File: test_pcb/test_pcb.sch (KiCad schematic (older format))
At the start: 69 parts, among them K0 KEYSW, K1 KEYSW, K10 KEYSW, K12 KEYSW, K13 KEYSW, K14 KEYSW, K15 KEYSW, K16 KEYSW, K17 KEYSW, K18 KEYSW, K2 KEYSW, K20 KEYSW, K21 KEYSW, K22 KEYSW, K3 KEYSW, K4 KEYSW, K5 KEYSW, K6 KEYSW, K7 KEYSW, K8 KEYSW, K9 KEYSW, P0 CONN_01X08, U0 Teensy3.2, U1 STP16CP05

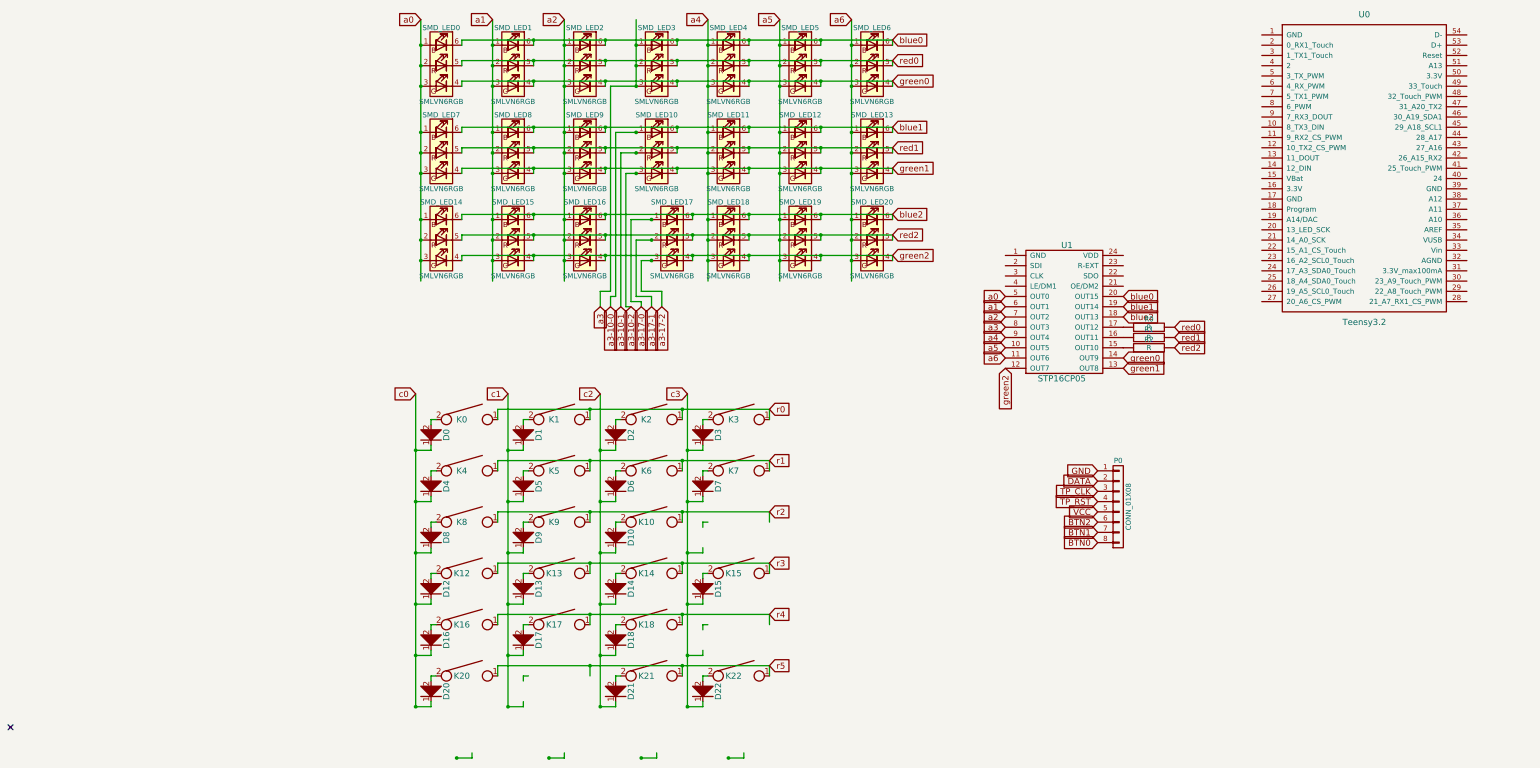
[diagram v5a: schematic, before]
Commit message: ground planes added
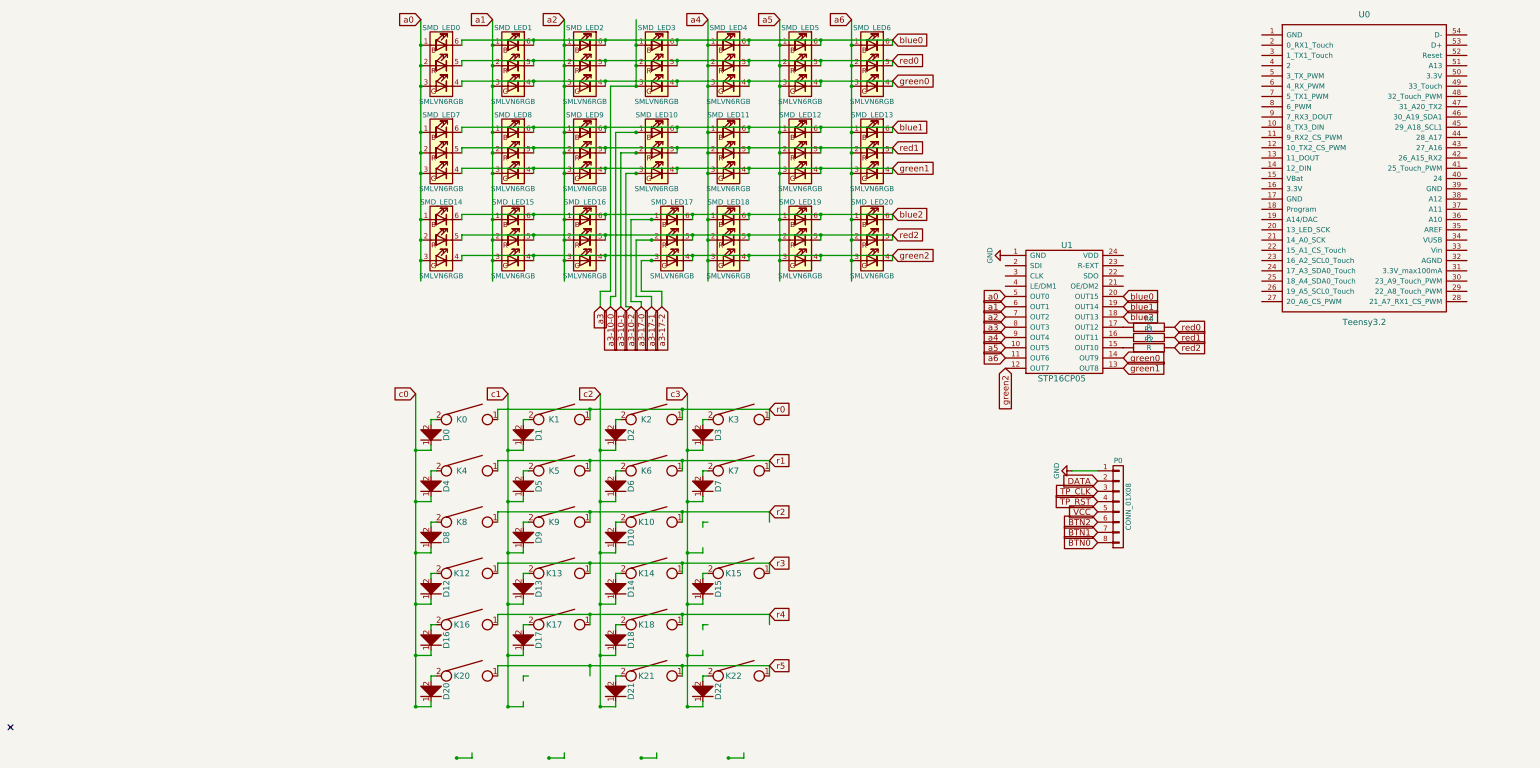
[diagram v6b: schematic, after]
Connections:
- wire segments 375 -> 243

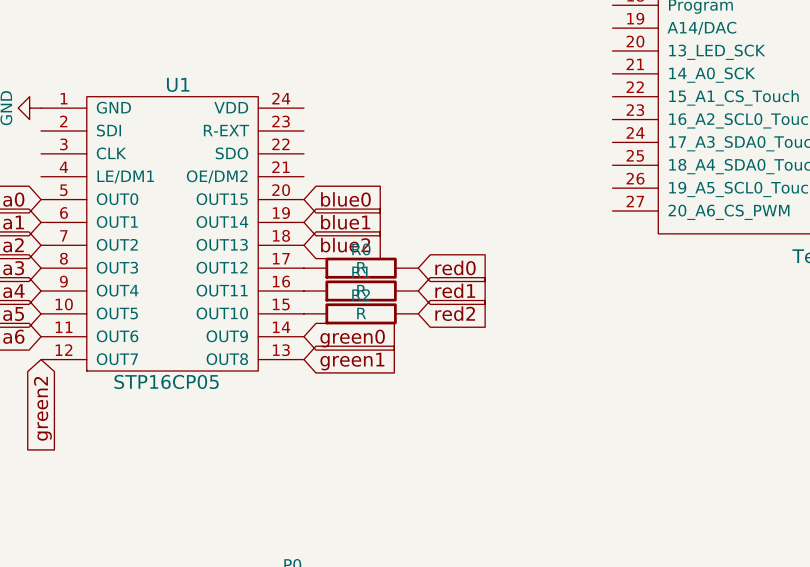
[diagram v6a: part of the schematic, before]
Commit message: when you use a contant current LED driver you don't actually need resistors!
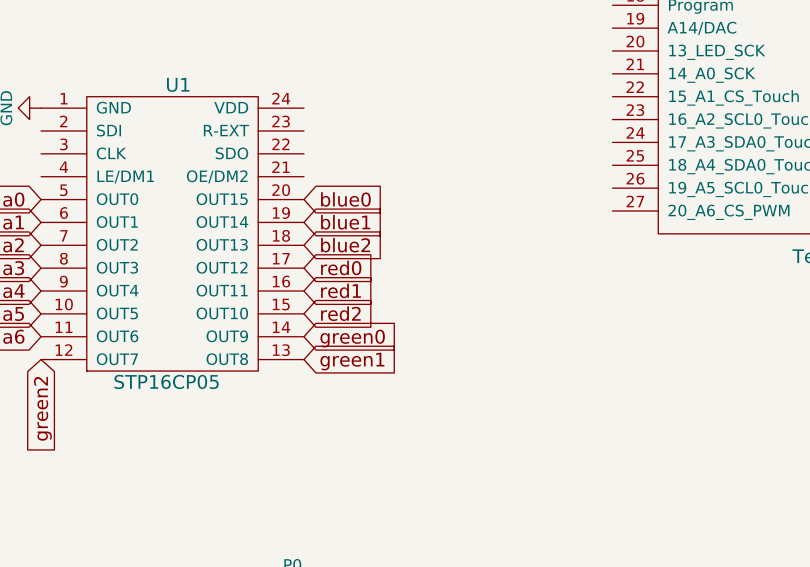
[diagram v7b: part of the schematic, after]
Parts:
- removed R0, R1, R2: R, Resistors_SMD:R_0603_HandSoldering, symbol R
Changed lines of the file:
@@
 Text GLabel 7650 3250 2    60   Input ~ 0
 blue0
-Text GLabel 8150 3550 2    60   Input ~ 0
+Text GLabel 7650 3550 2    60   Input ~ 0
 red0
 Text GLabel 7650 3850 2    60   Input ~ 0
@@
 Text GLabel 7650 3350 2    60   Input ~ 0
 blue1
-Text GLabel 8150 3650 2    60   Input ~ 0
+Text GLabel 7650 3650 2    60   Input ~ 0
 red1
 Text GLabel 7650 3950 2    60   Input ~ 0
@@
 Text GLabel 7650 3450 2    60   Input ~ 0
 blue2
-Text GLabel 8150 3750 2    60   Input ~ 0
+Text GLabel 7650 3750 2    60   Input ~ 0
 red2
 Text GLabel 6500 3950 3    60   Input ~ 0
@@
 Text GLabel 4200 6850 2    60   Input ~ 0
 r5
-$Comp
-L R R0
-U 1 1 58A20587
-P 7900 3550
-F 0 "R0" V 7980 3550 50  0000 C CNN
-F 1 "R" V 7900 3550 50  0000 C CNN
-F 2 "Resistors_SMD:R_0603_HandSoldering" H 7900 3550 60  0001 C CNN
-F 3 "" H 7900 3550 60  0000 C CNN
-	1    7900 3550
-	0    -1   -1   0
-$EndComp
-$Comp
-L R R1
-U 1 1 58A2074A
-P 7900 3650
-F 0 "R1" V 7980 3650 50  0000 C CNN
-F 1 "R" V 7900 3650 50  0000 C CNN
-F 2 "Resistors_SMD:R_0603_HandSoldering" H 7900 3650 60  0001 C CNN
-F 3 "" H 7900 3650 60  0000 C CNN
-	1    7900 3650
-	0    -1   -1   0
-$EndComp
-$Comp
-L R R2
-U 1 1 58A2088F
-P 7900 3750
-F 0 "R2" V 7980 3750 50  0000 C CNN
-F 1 "R" V 7900 3750 50  0000 C CNN
-F 2 "Resistors_SMD:R_0603_HandSoldering" H 7900 3750 60  0001 C CNN
-F 3 "" H 7900 3750 60  0000 C CNN
-	1    7900 3750
-	0    -1   -1   0
-$EndComp
 Text GLabel 2650 3350 3    60   Input ~ 0
 a3-10-0

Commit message: updates?
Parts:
- added P1, P2: CONN_01X08, Connectors_Molex:Molex_PicoBlade_53261-0871_08x1.25mm_Angled, symbol CONN_01X08
- added R0, R? (x2): R, symbol R
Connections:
- net labels added: +3.3V
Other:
- moved on the sheet: P0
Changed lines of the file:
@@
 L CONN_01X08 P0
 U 1 1 5897F60A
-P 7600 5300
-F 0 "P0" H 7600 5750 50  0000 C CNN
-F 1 "CONN_01X08" V 7700 5300 50  0000 C CNN
-F 2 "Connectors_Molex:Molex_PicoBlade_53261-0871_08x1.25mm_Angled" H 7600 5300 50  0001 C CNN
-F 3 "" H 7600 5300 50  0000 C CNN
-	1    7600 5300
-	1    0    0    -1
-$EndComp
-Text GLabel 7400 5650 0    60   Input ~ 0
+P 9900 5300
+F 0 "P0" H 9900 5750 50  0000 C CNN
+F 1 "CONN_01X08" V 10000 5300 50  0000 C CNN
+F 2 "Connectors_Molex:Molex_PicoBlade_53261-0871_08x1.25mm_Angled" H 9900 5300 50  0001 C CNN
+F 3 "" H 9900 5300 50  0000 C CNN
+	1    9900 5300
+	1    0    0    -1
+$EndComp
+Text GLabel 9700 5650 0    60   Input ~ 0
 BTN0
-Text GLabel 7400 5550 0    60   Input ~ 0
+Text GLabel 9700 5550 0    60   Input ~ 0
 BTN1
-Text GLabel 7400 5450 0    60   Input ~ 0
+Text GLabel 9700 5450 0    60   Input ~ 0
 BTN2
-Text GLabel 7400 5350 0    60   Input ~ 0
+Text GLabel 9700 5350 0    60   Input ~ 0
 VCC
-Text GLabel 7400 5050 0    60   Input ~ 0
+Text GLabel 9700 5050 0    60   Input ~ 0
 DATA
-Text GLabel 7400 5250 0    60   Input ~ 0
+Text GLabel 9700 5250 0    60   Input ~ 0
 TP_RST
-Text GLabel 7400 5150 0    60   Input ~ 0
+Text GLabel 9700 5150 0    60   Input ~ 0
 TP_CLK
 $Comp
@@
 Text GLabel 7650 3250 2    60   Input ~ 0
 blue0
-Text GLabel 7650 3550 2    60   Input ~ 0
+Text GLabel 8150 3550 2    60   Input ~ 0
 red0
 Text GLabel 7650 3850 2    60   Input ~ 0
@@
 Text GLabel 7650 3350 2    60   Input ~ 0
 blue1
-Text GLabel 7650 3650 2    60   Input ~ 0
+Text GLabel 8150 3650 2    60   Input ~ 0
 red1
 Text GLabel 7650 3950 2    60   Input ~ 0
@@
 Text GLabel 7650 3450 2    60   Input ~ 0
 blue2
-Text GLabel 7650 3750 2    60   Input ~ 0
+Text GLabel 8150 3750 2    60   Input ~ 0
 red2
 Text GLabel 6500 3950 3    60   Input ~ 0
@@
 a3-17-2
 $Comp
-L GND #PWR?
+L GND #PWR01
 U 1 1 58A59EDB
-P 7150 4950
-F 0 "#PWR?" H 7150 4700 50  0001 C CNN
-F 1 "GND" H 7150 4800 50  0000 C CNN
-F 2 "" H 7150 4950 50  0000 C CNN
-F 3 "" H 7150 4950 50  0000 C CNN
-	1    7150 4950
+P 9450 4950
+F 0 "#PWR01" H 9450 4700 50  0001 C CNN
+F 1 "GND" H 9450 4800 50  0000 C CNN
+F 2 "" H 9450 4950 50  0000 C CNN
+F 3 "" H 9450 4950 50  0000 C CNN
+	1    9450 4950
 	0    1    1    0
 $EndComp
 Wire Wire Line
-	7400 4950 7150 4950
-$Comp
-L GND #PWR?
+	9700 4950 9450 4950
+$Comp
+L GND #PWR02
 U 1 1 58A5AE89
 P 6500 2850
-F 0 "#PWR?" H 6500 2600 50  0001 C CNN
+F 0 "#PWR02" H 6500 2600 50  0001 C CNN
 F 1 "GND" H 6500 2700 50  0000 C CNN
 F 2 "" H 6500 2850 50  0000 C CNN
@@
 	0    1    1    0
 $EndComp
+Text GLabel 7750 5100 0    60   Input ~ 0
+a3-10-0
+Text GLabel 7750 5200 0    60   Input ~ 0
+a3-10-1
+Text GLabel 7750 5300 0    60   Input ~ 0
+a3-10-2
+Text GLabel 7750 5400 0    60   Input ~ 0
+a3-17-0
+Text GLabel 7750 5500 0    60   Input ~ 0
+a3-17-1
+Text GLabel 7750 5600 0    60   Input ~ 0
+a3-17-2
+$Comp
+L +3.3V #PWR03
+U 1 1 58A3C033
+P 7650 2850
+F 0 "#PWR03" H 7650 2700 50  0001 C CNN
+F 1 "+3.3V" H 7650 2990 50  0000 C CNN
+F 2 "" H 7650 2850 50  0000 C CNN
+F 3 "" H 7650 2850 50  0000 C CNN
+	1    7650 2850
+	0    1    1    0
+$EndComp
+$Comp
+L R R0
+U 1 1 58A3D228
+P 7900 3550
+F 0 "R0" V 7980 3550 50  0000 C CNN
+F 1 "R" V 7900 3550 50  0000 C CNN
+F 2 "" H 7900 3550 60  0000 C CNN
+F 3 "" H 7900 3550 60  0000 C CNN
+	1    7900 3550
+	0    1    1    0
+$EndComp
+$Comp
+L R R?
+U 1 1 58A3D3E0
+P 7900 3650
+F 0 "R?" V 7980 3650 50  0000 C CNN
+F 1 "R" V 7900 3650 50  0000 C CNN
+F 2 "" H 7900 3650 60  0000 C CNN
+F 3 "" H 7900 3650 60  0000 C CNN
+	1    7900 3650
+	0    1    1    0
+$EndComp
+$Comp
+L R R?
+U 1 1 58A3D4D0
+P 7900 3750
+F 0 "R?" V 7980 3750 50  0000 C CNN
+F 1 "R" V 7900 3750 50  0000 C CNN
+F 2 "" H 7900 3750 60  0000 C CNN
+F 3 "" H 7900 3750 60  0000 C CNN
+	1    7900 3750
+	0    1    1    0
+$EndComp
+$Comp
+L CONN_01X08 P1
+U 1 1 58A3B45B
+P 7950 5450
+F 0 "P1" H 7950 5900 50  0000 C CNN
+F 1 "CONN_01X08" V 8050 5450 50  0000 C CNN
+F 2 "Connectors_Molex:Molex_PicoBlade_53261-0871_08x1.25mm_Angled" H 7950 5450 50  0001 C CNN
+F 3 "" H 7950 5450 50  0000 C CNN
+	1    7950 5450
+	1    0    0    -1
+$EndComp
+$Comp
+L CONN_01X08 P2
+U 1 1 58A3CB40
+P 7950 6250
+F 0 "P2" H 7950 6700 50  0000 C CNN
+F 1 "CONN_01X08" V 8050 6250 50  0000 C CNN
+F 2 "Connectors_Molex:Molex_PicoBlade_53261-0871_08x1.25mm_Angled" H 7950 6250 50  0001 C CNN
+F 3 "" H 7950 6250 50  0000 C CNN
+	1    7950 6250
+	1    0    0    -1
+$EndComp
+Text GLabel 7750 5700 0    60   Input ~ 0
+blue1
+Text GLabel 7750 5800 0    60   Input ~ 0
+red1
+Text GLabel 7750 5900 0    60   Input ~ 0
+green1
+Text GLabel 7750 6000 0    60   Input ~ 0
+blue2
+Text GLabel 7750 6100 0    60   Input ~ 0
+red2
+Text GLabel 7800 6200 0    60   Input ~ 0
+green2
 $EndSCHEMATC
